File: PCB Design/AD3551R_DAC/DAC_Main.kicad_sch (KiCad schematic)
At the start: 1 part, among them U301 AD3551RBCPZ16

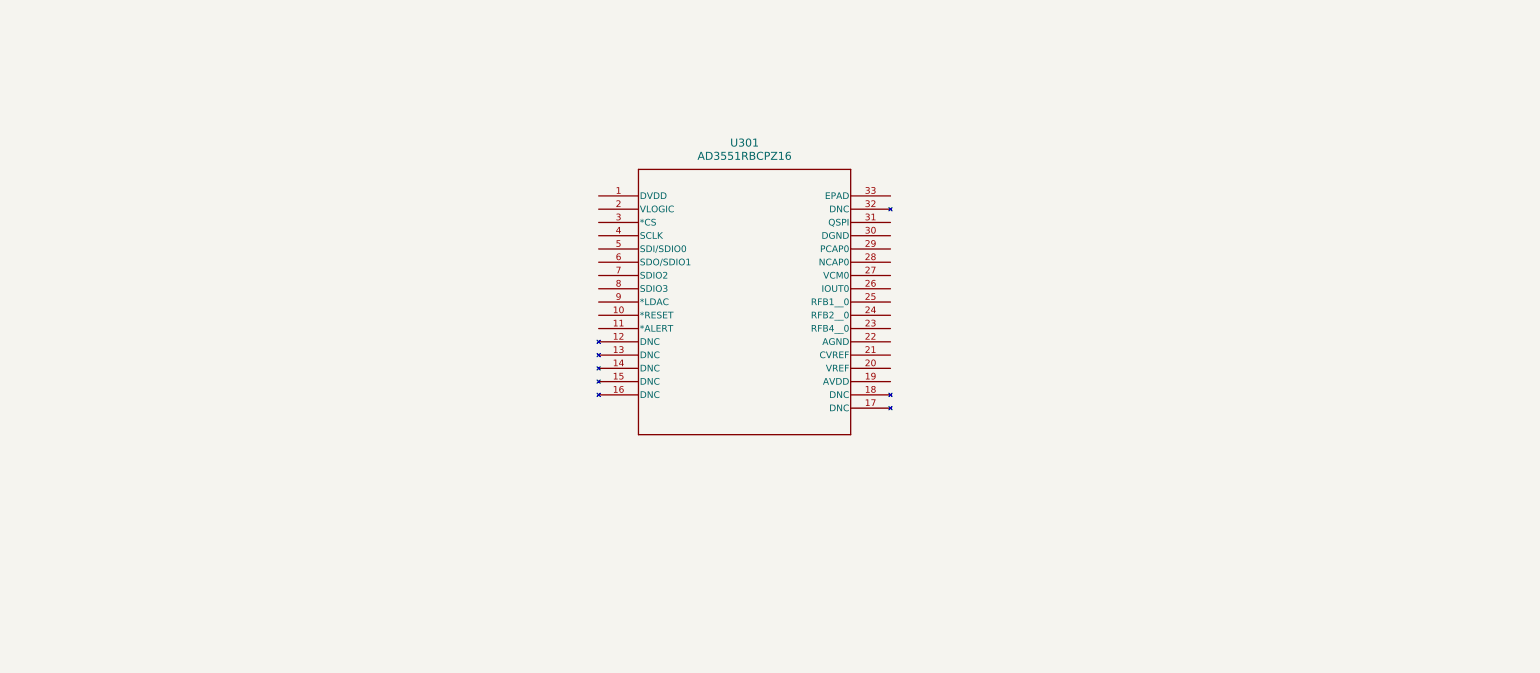
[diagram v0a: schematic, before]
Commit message: Schematic V1 Done and Up for Review
Schematic Done and into Review
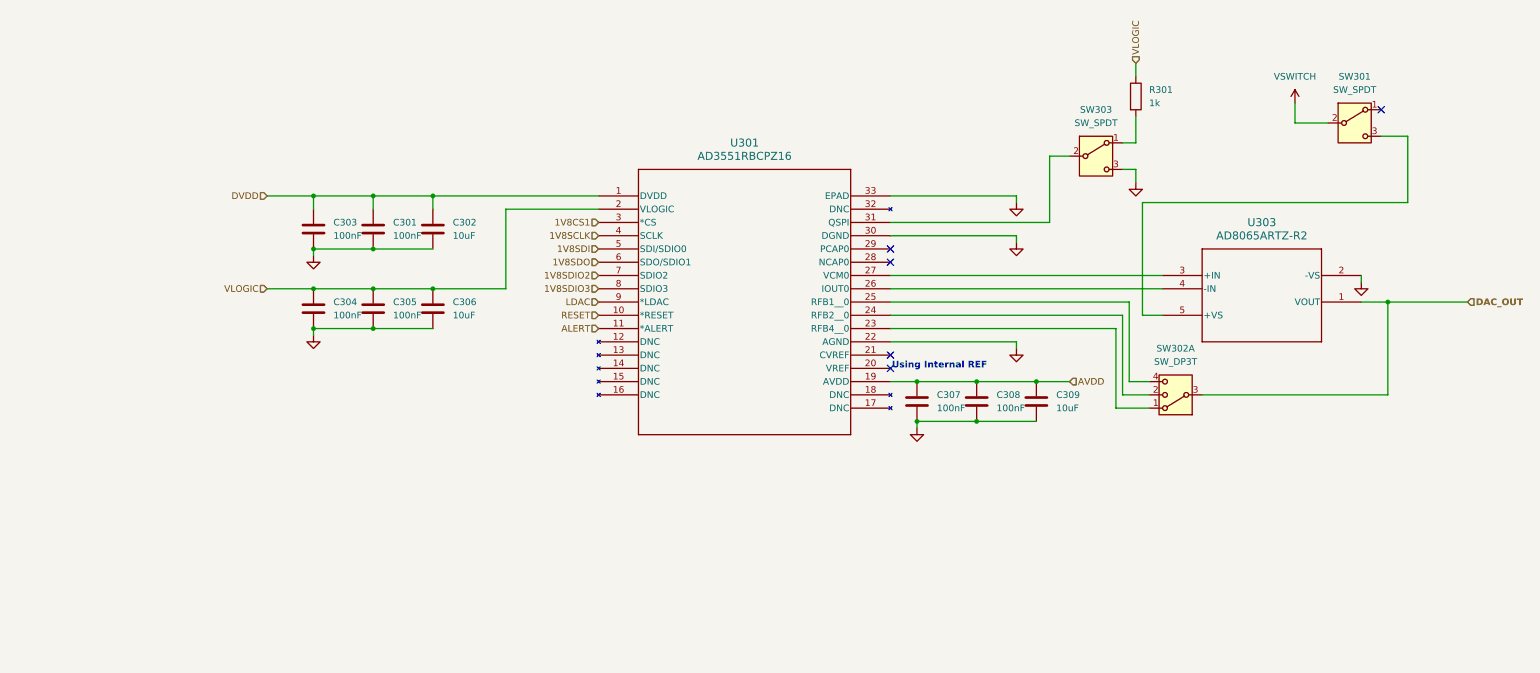
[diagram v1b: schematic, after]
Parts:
- added C301, C303, C304, C305, C307, C308: 100nF, symbol Device:C
- added C302, C306, C309: 10uF, symbol Device:C
- added R301: 1k, symbol Device:R
- added SW301, SW303: SW_SPDT, symbol Switch:SW_SPDT
- added SW302: SW_DP3T, symbol Switch:SW_DP3T
- added U303: AD8065ARTZ-R2, RJ_5_ADI, symbol Parts:AD8065ARTZ-R2
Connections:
- net DVDD: now reaches U301.1 (DVDD)
- net DVDD: now also C301.1, C302.1, C303.1
- net RESET: now reaches U301.10 (*RESET)
- net ALERT: now reaches U301.11 (*ALERT)
- net AVDD: now reaches U301.19 (AVDD)
- net AVDD: now also C307.1, C308.1, C309.1
- net VLOGIC: now reaches U301.2 (VLOGIC)
- net VLOGIC: now also C304.1, C305.1, C306.1, R301.1
- net GND: now reaches U301.22 (AGND)
- net GND: now also U301.30 (DGND), U301.33 (EPAD), C301.2, C302.2, C303.2, C304.2, C305.2, C306.2, C307.2, C308.2, C309.2, SW303.3 (C), U303.2 (-VS)
- net at U301.23 (RFB4__0): now also SW302.1
- net at U301.24 (RFB2__0): now also SW302.2
- net at U301.25 (RFB1__0): now also SW302.4
- net at U301.26 (IOUT0): now also U303.4 (-IN)
- net at U301.27 (VCM0): now also U303.3 (+IN)
- net 1V8CS1: now reaches U301.3 (*CS)
- net at U301.31 (QSPI): now also SW303.2 (B)
- net 1V8SCLK: now reaches U301.4 (SCLK)
- net 1V8SDI: now reaches U301.5 (SDI/SDIO0)
- net 1V8SDO: now reaches U301.6 (SDO/SDIO1)
- net 1V8SDIO2: now reaches U301.7 (SDIO2)
- net 1V8SDIO3: now reaches U301.8 (SDIO3)
- net LDAC: now reaches U301.9 (*LDAC)
- new net: SW301.3 (C), U303.5 (+VS)
- new net: R301.2, SW303.1 (A)
- new net DAC_OUT: SW302.3, U303.1 (VOUT)
- new net VSWITCH: SW301.2 (B)
- no-connect marks 0 -> 5
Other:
- note added: "Using Internal REF"

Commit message: decoupling
decoupling
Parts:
- added C310, C311: 100nF, symbol Device:C
- added C312: 10uF, symbol Device:C
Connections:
- net GND: now also C310.2, C311.2, C312.2
- net at SW301.3 (C), U303.5 (+VS): now also C310.1, C311.1, C312.1

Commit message: Changes
Changes
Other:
- note added: "Layout Notes: QFN Package Extend pads I_Out as short and thin as possible due to amplifier slew. Route Line with constant characteristic impedance for timing"
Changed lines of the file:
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@@
+		)
+	)
+	(text "Layout Notes: \n\nQFN Package Extend pads\n\nI_Out as short and thin as possible due to amplifier slew.\n\nRoute Line with constant characteristic impedance for timing"
+		(exclude_from_sim no)
+		(at 64.516 148.336 0)
+		(effects
+			(font
+				(size 2.54 2.54)
+				(thickness 0.508)
+				(bold yes)
+			)
 		)
 	)
@@
 		(at 257.81 62.23)
 		(diameter 0)
+		(color 255 255 0 1)
+	)
+	(junction
+		(at 48.26 73.66)
+		(diameter 0)
+		(color 0 0 194 1)
+	)
+	(junction
+		(at 269.24 85.09)
+		(diameter 0)
 		(color 0 0 0 0)
 	)
 	(junction
-		(at 48.26 73.66)
+		(at 71.12 73.66)
 		(diameter 0)
 		(color 0 0 194 1)
 	)
 	(junction
-		(at 269.24 85.09)
+		(at 163.83 116.84)
 		(diameter 0)
 		(color 0 0 0 0)
 	)
 	(junction
-		(at 71.12 73.66)
+		(at 254 93.98)
+		(diameter 0)
+		(color 255 153 0 1)
+	)
+	(junction
+		(at 59.69 91.44)
 		(diameter 0)
 		(color 0 0 194 1)
 	)
 	(junction
-		(at 163.83 116.84)
+		(at 175.26 116.84)
 		(diameter 0)
 		(color 0 0 0 0)
 	)
 	(junction
-		(at 254 93.98)
-		(diameter 0)
-		(color 255 153 0 1)
-	)
-	(junction
-		(at 59.69 91.44)
+		(at 186.69 109.22)
+		(diameter 0)
+		(color 255 0 255 1)
+	)
+	(junction
+		(at 71.12 91.44)
 		(diameter 0)
 		(color 0 0 194 1)
 	)
 	(junction
-		(at 175.26 116.84)
+		(at 163.83 109.22)
+		(diameter 0)
+		(color 255 0 255 1)
+	)
+	(junction
+		(at 59.69 83.82)
 		(diameter 0)
 		(color 0 0 0 0)
 	)
 	(junction
-		(at 186.69 109.22)
+		(at 175.26 109.22)
 		(diameter 0)
 		(color 255 0 255 1)
 	)
 	(junction
-		(at 71.12 91.44)
+		(at 59.69 73.66)
 		(diameter 0)
 		(color 0 0 194 1)
 	)
 	(junction
-		(at 163.83 109.22)
-		(diameter 0)
-		(color 255 0 255 1)
-	)
-	(junction
-		(at 59.69 83.82)
+		(at 261.62 73.66)
+		(diameter 0)
+		(color 255 255 0 1)
+	)
+	(junction
+		(at 48.26 99.06)
 		(diameter 0)
 		(color 0 0 0 0)
 	)
 	(junction
-		(at 175.26 109.22)
-		(diameter 0)
-		(color 255 0 255 1)
-	)
-	(junction
-		(at 59.69 73.66)
-		(diameter 0)
-		(color 0 0 194 1)
-	)
-	(junction
-		(at 261.62 73.66)
-		(diameter 0)
-		(color 0 0 0 0)
-	)
-	(junction
-		(at 48.26 99.06)
-		(diameter 0)
-		(color 0 0 0 0)
-	)
-	(junction
 		(at 261.62 62.23)
 		(diameter 0)
-		(color 0 0 0 0)
+		(color 255 255 0 1)
 	)
 	(junction
@@
 		)
 		(stroke
-			(width 0)
-			(type default)
+			(width 0.508)
+			(type default)
+			(color 255 255 0 1)
 		)
 	)
@@
 		)
 		(stroke
-			(width 0)
-			(type default)
+			(width 0.508)
+			(type default)
+			(color 0 0 255 1)
 		)
 	)
@@
 		)
 		(stroke
-			(width 0)
-			(type default)
+			(width 0.508)
+			(type default)
+			(color 255 255 0 1)
 		)
 	)
@@
 		)
 		(stroke
-			(width 0)
-			(type default)
+			(width 0.508)
+			(type default)
+			(color 0 0 255 1)
 		)
 	)
@@
 		)
 		(stroke
-			(width 0)
-			(type default)
+			(width 0.508)
+			(type default)
+			(color 255 255 0 1)
 		)
 	)
@@
 		)
 		(stroke
-			(width 0)
-			(type default)
+			(width 0.508)
+			(type default)
+			(color 255 255 0 1)
 		)
 	)
@@
 	(wire
 		(pts
-			(xy 207.01 96.52) (xy 207.01 74.93)
-		)
-		(stroke
-			(width 0)
-			(type default)
+			(xy 208.28 96.52) (xy 208.28 74.93)
+		)
+		(stroke
+			(width 0.508)
+			(type default)
+			(color 255 255 0 1)
 		)
 	)
@@
 	(wire
 		(pts
-			(xy 207.01 74.93) (xy 257.81 74.93)
-		)
-		(stroke
-			(width 0)
-			(type default)
+			(xy 208.28 74.93) (xy 257.81 74.93)
+		)
+		(stroke
+			(width 0.508)
+			(type default)
+			(color 255 255 0 1)
 		)
 	)
@@
 		)
 		(stroke
-			(width 0)
-			(type default)
+			(width 0.508)
+			(type default)
+			(color 255 255 0 1)
 		)
 	)
@@
 		)
 		(stroke
-			(width 0)
-			(type default)
+			(width 0.508)
+			(type default)
+			(color 255 255 0 1)
 		)
 	)
@@
 		)
 		(stroke
-			(width 0)
-			(type default)
+			(width 0.508)
+			(type default)
+			(color 0 0 255 1)
 		)
 	)
@@
 		)
 		(stroke
-			(width 0)
-			(type default)
+			(width 0.508)
+			(type default)
+			(color 255 255 0 1)
 		)
 	)
@@
 	(wire
 		(pts
-			(xy 210.82 96.52) (xy 207.01 96.52)
-		)
-		(stroke
-			(width 0)
-			(type default)
-		)
-	)
+			(xy 210.82 96.52) (xy 208.28 96.52)
+		)
+		(stroke
+			(width 0.508)
+			(type default)
+			(color 255 255 0 1)
+		)
+	)

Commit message: PCB
PCB Layout started
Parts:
- C301, C303, C304, C305, C307, C308, C310, C311: footprint (none) -> Capacitor_SMD:C_0603_1608Metric
- C302, C306, C309, C312: footprint (none) -> Capacitor_SMD:C_0805_2012Metric_Pad1.18x1.45mm_HandSolder
- R301: footprint (none) -> Resistor_SMD:R_1206_3216Metric_Pad1.30x1.75mm_HandSolder
- SW301, SW303: footprint (none) -> Parts_fab:toggle_switch
- SW302: footprint (none) -> Parts_fab:3_way_switch_CUS-13TB_NDC
- U301: footprint CP-32-30_ADI -> Parts_fab:AD3551R
- U303: footprint RJ_5_ADI -> Parts_fab:AD8065
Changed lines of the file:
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@@
 			)
 		)
-		(property "Footprint" ""
+		(property "Footprint" "Capacitor_SMD:C_0603_1608Metric"
 			(at 60.6552 83.82 0)
 			(hide yes)
@@
 			)
 		)
-		(property "Footprint" ""
+		(property "Footprint" "Capacitor_SMD:C_0603_1608Metric"
 			(at 269.24 72.6948 0)
 			(hide yes)
@@
 			)
 		)
-		(property "Footprint" ""
+		(property "Footprint" "Capacitor_SMD:C_0603_1608Metric"
 			(at 49.2252 83.82 0)
 			(hide yes)
@@
 			)
 		)
-		(property "Footprint" ""
+		(property "Footprint" "Parts_fab:toggle_switch"
 			(at 247.65 59.69 0)
 			(hide yes)
@@
 			)
 		)
-		(property "Footprint" ""
+		(property "Footprint" "Capacitor_SMD:C_0603_1608Metric"
 			(at 49.2252 99.06 0)
 			(hide yes)
@@
 			)
 		)
-		(property "Footprint" ""
+		(property "Footprint" "Capacitor_SMD:C_0603_1608Metric"
 			(at 176.2252 116.84 0)
 			(hide yes)
@@
 			)
 		)
-		(property "Footprint" ""
+		(property "Footprint" "Capacitor_SMD:C_0805_2012Metric_Pad1.18x1.45mm_HandSolder"
 			(at 72.0852 99.06 0)
 			(hide yes)
@@
 			)
 		)
-		(property "Footprint" ""
+		(property "Footprint" "Parts_fab:toggle_switch"
 			(at 198.12 66.04 0)
 			(hide yes)
@@
 			)
 		)
-		(property "Footprint" "CP-32-30_ADI"
+		(property "Footprint" "Parts_fab:AD3551R"
 			(at 102.87 73.66 0)
 			(hide yes)
@@
 			)
 		)
-		(property "Footprint" ""
+		(property "Footprint" "Capacitor_SMD:C_0603_1608Metric"
 			(at 269.24 61.2648 0)
 			(hide yes)
@@
 			)
 		)
-		(property "Footprint" ""
+		(property "Footprint" "Capacitor_SMD:C_0603_1608Metric"
 			(at 164.7952 116.84 0)
 			(hide yes)
@@
 			)
 		)
-		(property "Footprint" "RJ_5_ADI"
+		(property "Footprint" "Parts_fab:AD8065"
 			(at 210.82 88.9 0)
 			(hide yes)
@@
 			)
 		)
-		(property "Footprint" ""
+		(property "Footprint" "Parts_fab:3_way_switch_CUS-13TB_NDC"
 			(at 229.235 116.205 0)
 			(hide yes)
@@
 			)
 		)
-		(property "Footprint" ""
+		(property "Footprint" "Capacitor_SMD:C_0603_1608Metric"
 			(at 60.6552 99.06 0)
 			(hide yes)
@@
 			)
 		)
-		(property "Footprint" ""
+		(property "Footprint" "Capacitor_SMD:C_0805_2012Metric_Pad1.18x1.45mm_HandSolder"
 			(at 269.24 84.1248 0)
 			(hide yes)
@@
 			)
 		)
-		(property "Footprint" ""
+		(property "Footprint" "Capacitor_SMD:C_0805_2012Metric_Pad1.18x1.45mm_HandSolder"
 			(at 187.6552 116.84 0)
 			(hide yes)
@@
 			)
 		)
-		(property "Footprint" ""
+		(property "Footprint" "Resistor_SMD:R_1206_3216Metric_Pad1.30x1.75mm_HandSolder"
 			(at 203.962 54.61 90)
 			(hide yes)
@@
 			)
 		)
-		(property "Footprint" ""
+		(property "Footprint" "Capacitor_SMD:C_0805_2012Metric_Pad1.18x1.45mm_HandSolder"
 			(at 72.0852 83.82 0)
 			(hide yes)

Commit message: Routing Done
Routing Done
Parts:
- removed SW302: SW_DP3T, Parts_fab:3_way_switch_CUS-13TB_NDC, symbol Switch:SW_DP3T
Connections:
- net DAC_OUT: now also U301.24 (RFB2__0)
- no-connect marks 5 -> 7
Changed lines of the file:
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@@
+	)
+	(no_connect
+		(at 208.28 109.22)
+	)
+	(no_connect
+		(at 208.28 114.3)
 	)
 	(no_connect
@@
 	(wire
 		(pts
-			(xy 203.2 111.76) (xy 208.28 111.76)
+			(xy 203.2 111.76) (xy 254 111.76)
 		)
 		(stroke
@@
 			(width 0)
 			(type default)
-		)
-	)
-	(wire
-		(pts
-			(xy 218.44 111.76) (xy 254 111.76)
-		)
-		(stroke
-			(width 0.508)
-			(type default)
-			(color 255 153 0 1)
 		)
 	)
@@
 					(unit 1)
 				)
-			)
-		)
-	)
-	(symbol
-		(lib_id "Switch:SW_DP3T")
-		(at 213.36 111.76 180)
-		(unit 1)
-		(body_style 1)
-		(exclude_from_sim no)
-		(in_bom yes)
-		(on_board yes)
-		(in_pos_files yes)
-		(dnp no)
-		(fields_autoplaced yes)
-		(property "Reference" "SW302"
-			(at 213.36 102.87 0)
-			(show_name no)
-			(do_not_autoplace no)
-			(effects
-				(font
-					(size 1.27 1.27)
-				)
-			)
-		)
-		(property "Value" "SW_DP3T"
-			(at 213.36 105.41 0)
-			(show_name no)
-			(do_not_autoplace no)
-			(effects
-				(font
-					(size 1.27 1.27)
-				)
-			)
-		)
-		(property "Footprint" "Parts_fab:3_way_switch_CUS-13TB_NDC"
-			(at 229.235 116.205 0)
-			(hide yes)
-			(show_name no)
-			(do_not_autoplace no)
-			(effects
-				(font
-					(size 1.27 1.27)
-				)
-			)
-		)
-		(property "Datasheet" ""
-			(at 229.235 116.205 0)
-			(hide yes)
-			(show_name no)
-			(do_not_autoplace no)
-			(effects
-				(font
-					(size 1.27 1.27)
-				)
-			)
-		)
-		(property "Description" "Switch, three position, dual pole triple throw, 3 position switch, SP3T"
-			(at 213.36 111.76 0)
-			(hide yes)
-			(show_name no)
-			(do_not_autoplace no)
-			(effects
-				(font
-					(size 1.27 1.27)
-				)
-			)
-		)
-		(pin "7"
-		)
-		(pin "3"
-		)
-		(pin "4"
-		)
-		(pin "1"
-		)
-		(pin "5"
-		)
-		(pin "8"
-		)
-		(pin "2"
-		)
-		(pin "6"
-		)
-		(instances
-			(project "AD3551R_DAC"
-				(path "/3d4144e0-3656-4efa-94fd-8cd1f0e2cd3f/d70c20e7-6db8-4174-a944-0619e976b5fb"
-					(reference "SW302")
-					(unit 1)
-				)

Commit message: small changes
small changes
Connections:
- net DAC_OUT: now also U301.23 (RFB4__0); no longer U301.24 (RFB2__0)
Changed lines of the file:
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@@
-	)
-	(no_connect
-		(at 208.28 114.3)
 	)
 	(no_connect
@@
 	)
 	(no_connect
+		(at 208.28 111.76)
+	)
+	(no_connect
 		(at 158.75 83.82)
 	)
@@
 	(wire
 		(pts
-			(xy 203.2 111.76) (xy 254 111.76)
+			(xy 203.2 111.76) (xy 208.28 111.76)
 		)
 		(stroke
@@
 	(wire
 		(pts
-			(xy 201.93 114.3) (xy 208.28 114.3)
+			(xy 201.93 114.3) (xy 254 114.3)
 		)
 		(stroke
@@
 	(wire
 		(pts
-			(xy 254 111.76) (xy 254 93.98)
-		)
-		(stroke
+			(xy 254 93.98) (xy 254 114.3)
+		)
+		(stroke
